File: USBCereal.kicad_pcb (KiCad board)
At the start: 2 copper layers, 25.1 x 19.6 mm, 18 parts, among them J1 USB_C, J2 Conn_01x06, U1 XC6206P332MR, U2 CH340C

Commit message: finalise fabrication files, read for JLCPCB order
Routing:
- net GNDD: vias 7 -> 8
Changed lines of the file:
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@@
     (thickness 1.6)
     (drawings 19)
-    (tracks 134)
+    (tracks 133)
     (zones 0)
     (modules 18)
@@
   (segment (start 27.794 23.801) (end 28.3972 23.1978) (width 0.5) (layer F.Cu) (net 2))
   (segment (start 28.3972 23.1978) (end 28.3972 22.047184) (width 0.5) (layer F.Cu) (net 2))
-  (via (at 24.2316 30.0228) (size 0.8) (drill 0.4) (layers F.Cu B.Cu) (net 2))
-  (via (at 24.2316 24.13) (size 0.8) (drill 0.4) (layers F.Cu B.Cu) (net 2))
-  (via (at 24.2316 27.0764) (size 0.8) (drill 0.4) (layers F.Cu B.Cu) (net 2))
   (via (at 40.894 19.05) (size 0.8) (drill 0.4) (layers F.Cu B.Cu) (net 2))
   (via (at 30.734 32.004) (size 0.8) (drill 0.4) (layers F.Cu B.Cu) (net 2))
+  (via (at 22.86 24.13) (size 0.8) (drill 0.4) (layers F.Cu B.Cu) (net 2))
+  (via (at 22.86 25.908) (size 0.8) (drill 0.4) (layers F.Cu B.Cu) (net 2))
+  (via (at 22.86 27.686) (size 0.8) (drill 0.4) (layers F.Cu B.Cu) (net 2))
+  (via (at 22.86 29.464) (size 0.8) (drill 0.4) (layers F.Cu B.Cu) (net 2))
   (segment (start 34.549847 24.705847) (end 34.544 24.7) (width 0.3) (layer F.Cu) (net 3))
   (segment (start 36.195 28.702) (end 36.195 29.464) (width 0.3) (layer F.Cu) (net 3))
@@
   (segment (start 40.8835 32.305) (end 40.894 32.2945) (width 0.25) (layer F.Cu) (net 12))
   (segment (start 39.116 32.305) (end 40.8835 32.305) (width 0.25) (layer F.Cu) (net 12))
-  (segment (start 27.794 28.801) (end 26.628002 28.801) (width 0.25) (layer F.Cu) (net 13))
-  (segment (start 26.628002 28.801) (end 26.138003 29.290999) (width 0.25) (layer F.Cu) (net 13))
+  (segment (start 25.50399 32.74489) (end 26.0585 33.2994) (width 0.25) (layer F.Cu) (net 13))
+  (segment (start 26.526998 28.801) (end 25.50399 29.824008) (width 0.25) (layer F.Cu) (net 13))
   (segment (start 25.50399 29.824008) (end 25.50399 32.74489) (width 0.25) (layer F.Cu) (net 13))
-  (segment (start 26.138003 29.290999) (end 26.036999 29.290999) (width 0.25) (layer F.Cu) (net 13))
-  (segment (start 25.50399 32.74489) (end 26.0585 33.2994) (width 0.25) (layer F.Cu) (net 13))
-  (segment (start 26.036999 29.290999) (end 25.50399 29.824008) (width 0.25) (layer F.Cu) (net 13))
+  (segment (start 27.794 28.801) (end 26.526998 28.801) (width 0.25) (layer F.Cu) (net 13))
   (segment (start 27.793 25.801) (end 27.768001 25.825999) (width 0.25) (layer F.Cu) (net 14))
   (segment (start 27.794 25.801) (end 27.793 25.801) (width 0.25) (layer F.Cu) (net 14))

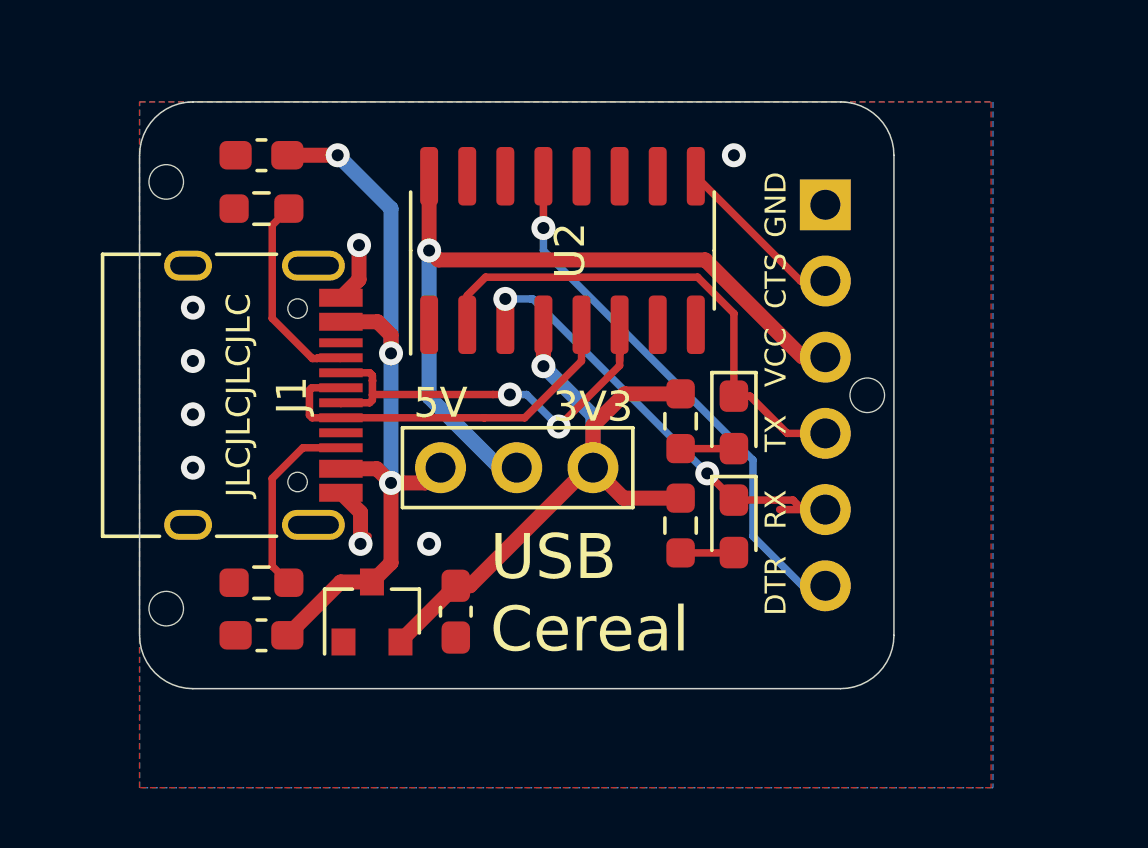
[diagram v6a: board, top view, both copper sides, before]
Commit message: Redsigned the pcb to use a switch rather than a jumper for the selection of the supply voltage
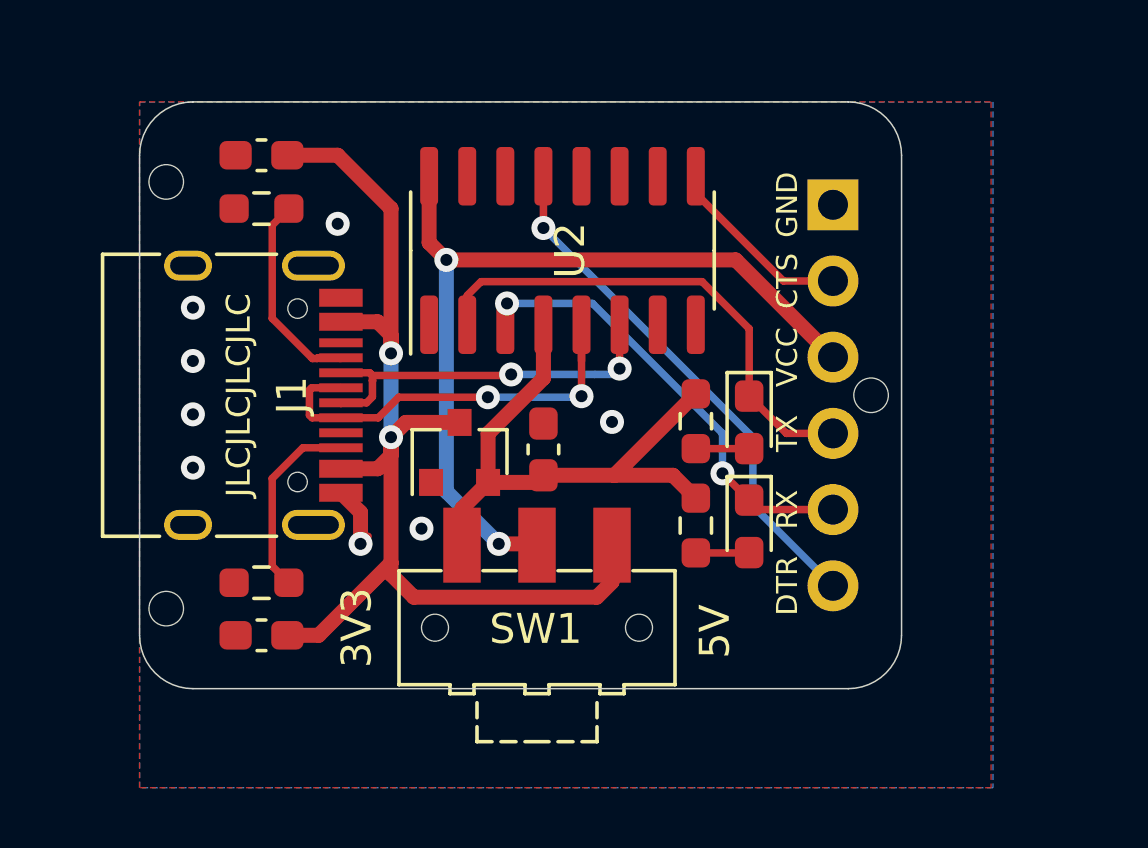
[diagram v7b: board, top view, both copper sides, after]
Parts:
- removed JP1: Jumper, Connector_PinHeader_2.54mm:PinHeader_1x03_P2.54mm_Vertical
- added SW1: SW_SPDT, Button_Switch_SMD:SW_SPDT_CK-JS102011SAQN, F.Cu at (34.3, 34.8)
- moved C3 6.15 mm to (34.5, 28.9), turned to 90 degrees
- moved U1 6.07 mm to (31.8, 29.0)
- moved D1 0.51 mm to (41.4, 28.0)
- moved D2 0.51 mm to (41.4, 31.4)
- moved R3 0.51 mm to (39.6, 27.9)
- moved R4 0.51 mm to (39.6, 31.4)
- moved J2 0.25 mm to (44.2, 20.7)
- moved REF** 0.13 mm to (45.5, 27.1)
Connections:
- J1 pad A8: (no net) -> Net-(J1-PadA8)
- J1 pad B8: (no net) -> Net-(J1-PadB8)
- U2 pad 10: (no net) -> Net-(U2-Pad10)
- U2 pad 11: (no net) -> Net-(U2-Pad11)
- U2 pad 12: (no net) -> Net-(U2-Pad12)
- U2 pad 14: (no net) -> Net-(U2-Pad14)
- U2 pad 15: (no net) -> Net-(U2-Pad15)
- U2 pad 7: (no net) -> Net-(U2-Pad7)
- U2 pad 8: (no net) -> Net-(U2-Pad8)
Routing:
- net +5V: track 27.1 -> 37.4 mm, vias 3 -> 2
- net VCC: track 25.2 -> 28.7 mm, vias 1 -> 2
- net +3V3: track 23.2 -> 19.7 mm, vias 1 -> 0
- net /USB_D-: track 16.2 -> 12.9 mm
- net GNDD: track 4.34 -> 2.33 mm
- net /USB_D+: track 13.0 -> 14.9 mm, vias 0 -> 2
- net /CTS: track 5.00 -> 6.35 mm
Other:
- board size 25.1 x 19.6 mm -> 25.4 x 19.6 mm

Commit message: update logo placment
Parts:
- moved G*** 1.78 mm to (35.8, 24.6)
